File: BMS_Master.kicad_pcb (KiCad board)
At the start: 2 copper layers, 65 x 45 mm, 84 parts, among them J1 PWR, J2 PROG, J3 BMS_M_OUT, J4 BMS_M_IN, J5 CAN, Q1 BC807, SW1 SW_SPST, U1 AP2204K-ADJ, U2 AP2204K-ADJ, U3 STM32F103C8Tx, U4 BQ79600-Q1, U5 SN65HVD256D, Y1 8M, Y2 32.768k

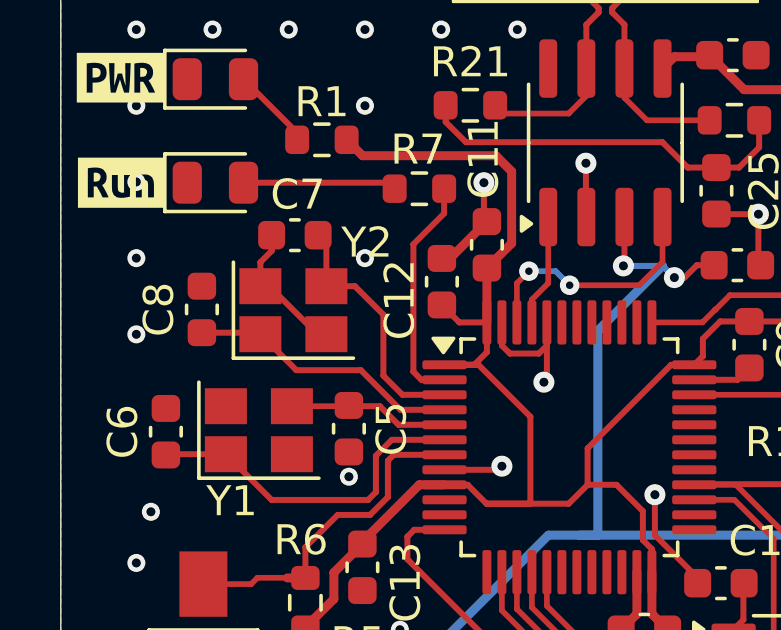
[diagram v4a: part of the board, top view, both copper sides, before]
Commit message: Fix crystal pinout connection
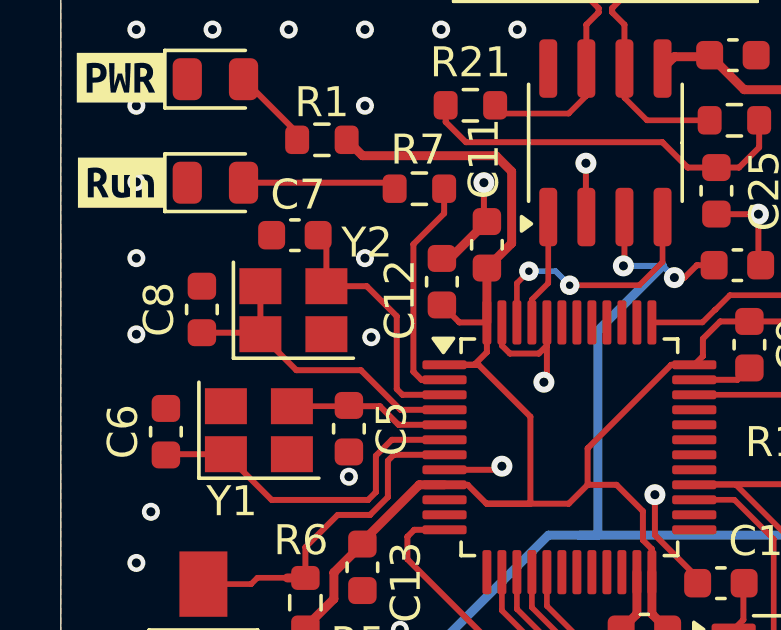
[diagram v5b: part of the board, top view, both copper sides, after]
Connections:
- net Net-(U3-PC14) renamed /LSE_IN
- C8 pad 1: Net-(U3-PC15) -> /LSE_OUT
- U3 pad 4: Net-(U3-PC15) -> /LSE_OUT
- Y2 pad 1: Net-(U3-PC15) -> /LSE_OUT
- Y2 pad 4: GND -> /LSE_OUT
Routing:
- net /LSE_OUT: track 0.00 -> 10.8 mm
- net Net-(U3-PC15): track 9.15 -> 0.00 mm
- net GND: track 37.1 -> 32.7 mm, vias 105 -> 106
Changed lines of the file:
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@@
   (net 5 "Net-(U3-PD0)")
   (net 6 "Net-(U3-PD1)")
-  (net 7 "Net-(U3-PC14)")
-  (net 8 "Net-(U3-PC15)")
+  (net 7 "/LSE_IN")
+  (net 8 "/LSE_OUT")
   (net 9 "Net-(U4-DVDD)")
   (net 10 "COMHP")
@@
       (stroke (width 0.1) (type solid)) (layer "F.Fab"))
     (pad "1" smd rect (at -1.1 0.8) (size 1.4 1.2) (layers "F.Cu" "F.Paste" "F.Mask")
-      (net 8 "Net-(U3-PC15)") (pinfunction "1") (pintype "passive"))
+      (net 8 "/LSE_OUT") (pinfunction "1") (pintype "passive"))
     (pad "2" smd rect (at 1.1 0.8) (size 1.4 1.2) (layers "F.Cu" "F.Paste" "F.Mask")
       (net 1 "GND") (pinfunction "2") (pintype "passive"))
     (pad "3" smd rect (at 1.1 -0.8) (size 1.4 1.2) (layers "F.Cu" "F.Paste" "F.Mask")
-      (net 7 "Net-(U3-PC14)") (pinfunction "3") (pintype "passive"))
+      (net 7 "/LSE_IN") (pinfunction "3") (pintype "passive"))
     (pad "4" smd rect (at -1.1 -0.8) (size 1.4 1.2) (layers "F.Cu" "F.Paste" "F.Mask")
-      (net 1 "GND") (pinfunction "4") (pintype "passive"))
+      (net 8 "/LSE_OUT") (pinfunction "4") (pintype "passive"))
     (model "${KICAD6_3DMODEL_DIR}/Crystal.3dshapes/Crystal_SMD_SeikoEpson_FA238-4Pin_3.2x2.5mm.wrl"
       (offset (xyz 0 0 0))
@@
       (net 33 "RUN_LED") (pinfunction "PC13") (pintype "bidirectional"))
     (pad "3" smd roundrect (at -4.1625 -1.75) (size 1.475 0.3) (layers "F.Cu" "F.Paste" "F.Mask") (roundrect_rratio 0.25)
-      (net 7 "Net-(U3-PC14)") (pinfunction "PC14") (pintype "bidirectional"))
+      (net 7 "/LSE_IN") (pinfunction "PC14") (pintype "bidirectional"))
     (pad "4" smd roundrect (at -4.1625 -1.25) (size 1.475 0.3) (layers "F.Cu" "F.Paste" "F.Mask") (roundrect_rratio 0.25)
-      (net 8 "Net-(U3-PC15)") (pinfunction "PC15") (pintype "bidirectional"))
+      (net 8 "/LSE_OUT") (pinfunction "PC15") (pintype "bidirectional"))
     (pad "5" smd roundrect (at -4.1625 -0.75) (size 1.475 0.3) (layers "F.Cu" "F.Paste" "F.Mask") (roundrect_rratio 0.25)
       (net 5 "Net-(U3-PD0)") (pinfunction "PD0") (pintype "bidirectional"))
@@
       (stroke (width 0.1) (type solid)) (layer "F.Fab"))
     (pad "1" smd roundrect (at -0.775 0 90) (size 0.9 0.95) (layers "F.Cu" "F.Paste" "F.Mask") (roundrect_rratio 0.25)
-      (net 8 "Net-(U3-PC15)") (pintype "passive"))
+      (net 8 "/LSE_OUT") (pintype "passive"))
     (pad "2" smd roundrect (at 0.775 0 90) (size 0.9 0.95) (layers "F.Cu" "F.Paste" "F.Mask") (roundrect_rratio 0.25)
       (net 1 "GND") (pintype "passive"))
@@
       (stroke (width 0.1) (type solid)) (layer "F.Fab"))
     (pad "1" smd roundrect (at -0.775 0 180) (size 0.9 0.95) (layers "F.Cu" "F.Paste" "F.Mask") (roundrect_rratio 0.25)
-      (net 7 "Net-(U3-PC14)") (pintype "passive"))
+      (net 7 "/LSE_IN") (pintype "passive"))
     (pad "2" smd roundrect (at 0.775 0 180) (size 0.9 0.95) (layers "F.Cu" "F.Paste" "F.Mask") (roundrect_rratio 0.25)
       (net 1 "GND") (pintype "passive"))
@@
   (segment (start 87.36 55.25) (end 87.355 55.245) (width 0.2) (layer "F.Cu") (net 1))
   (segment (start 80.085 63.77) (end 78.2925 63.77) (width 0.2) (layer "F.Cu") (net 1))
+  (segment (start 74.355 59.25) (end 74.055 59.25) (width 0.2) (layer "F.Cu") (net 1))
   (segment (start 84.705 68.575) (end 84.705 67.1825) (width 0.3) (layer "F.Cu") (net 1))
   (segment (start 85.305 64.6) (end 85.305 65.946904) (width 0.2) (layer "F.Cu") (net 1))
@@
   (segment (start 86.73 67.371904) (end 86.73 67.55) (width 0.2) (layer "F.Cu") (net 1))
   (segment (start 78.205 56.725) (end 78.475 56.725) (width 0.3) (layer "F.Cu") (net 1))
-  (segment (start 72.53 56.475) (end 72.53 55.95) (width 0.2) (layer "F.Cu") (net 1))
   (segment (start 81.705 58.8575) (end 81.705 59.62741) (width 0.2) (layer "F.Cu") (net 1))
   (segment (start 82.875 72.57) (end 83.405 73.1) (width 0.2) (layer "F.Cu") (net 1))
@@
   (segment (start 88.755 56.875) (end 88.83 56.95) (width 0.2) (layer "F.Cu") (net 1))
   (segment (start 79.605 55.395) (end 79.705 55.495) (width 0.2) (layer "F.Cu") (net 1))
-  (segment (start 72.155 56.85) (end 72.53 56.475) (width 0.2) (layer "F.Cu") (net 1))
   (segment (start 81.43741 59.895) (end 80.47259 59.895) (width 0.2) (layer "F.Cu") (net 1))
   (segment (start 84.955 70.4) (end 84.18 69.625) (width 0.2) (layer "F.Cu") (net 1))
   (segment (start 84.18 69.625) (end 84.18 69.1) (width 0.2) (layer "F.Cu") (net 1))
-  (segment (start 72.455 57.65) (end 74.055 59.25) (width 0.2) (layer "F.Cu") (net 1))
   (segment (start 83.005 53.55) (end 83.005 55.33) (width 0.2) (layer "F.Cu") (net 1))
   (segment (start 85.305 65.946904) (end 86.73 67.371904) (width 0.2) (layer "F.Cu") (net 1))
@@
   (segment (start 88.06 60.77) (end 86.6175 60.77) (width 0.2) (layer "F.Cu") (net 1))
   (segment (start 88.455 60.375) (end 88.06 60.77) (width 0.2) (layer "F.Cu") (net 1))
-  (segment (start 74.055 59.25) (end 74.355 59.25) (width 0.2) (layer "F.Cu") (net 1))
   (segment (start 95.355 74.07) (end 96.005 74.07) (width 0.2) (layer "F.Cu") (net 1))
   (segment (start 88.755 55.25) (end 88.755 56.875) (width 0.2) (layer "F.Cu") (net 1))
   (segment (start 81.155 76.7875) (end 81.155 78.175) (width 0.3) (layer "F.Cu") (net 1))
   (segment (start 81.705 59.62741) (end 81.43741 59.895) (width 0.2) (layer "F.Cu") (net 1))
-  (segment (start 72.155 57.65) (end 72.455 57.65) (width 0.2) (layer "F.Cu") (net 1))
-  (segment (start 72.155 57.65) (end 72.155 56.85) (width 0.2) (layer "F.Cu") (net 1))
   (segment (start 81.155 78.175) (end 81.43 78.45) (width 0.3) (layer "F.Cu") (net 1))
   (segment (start 81.705 60.75) (end 81.705 58.8575) (width 0.2) (layer "F.Cu") (net 1))
@@
   (via (at 70.56 74.495) (size 0.6) (drill 0.3) (layers "F.Cu" "B.Cu") (free) (net 1))
   (via (at 78.18 46.555) (size 0.6) (drill 0.3) (layers "F.Cu" "B.Cu") (free) (net 1))
+  (via (at 75.85 59.35) (size 0.6) (drill 0.3) (layers "F.Cu" "B.Cu") (free) (net 1))
   (segment (start 80.205 76.125001) (end 80.555001 75.775) (width 0.3) (layer "F.Cu") (net 2))
   (segment (start 80.205 76.7875) (end 80.205 76.125001) (width 0.3) (layer "F.Cu") (net 2))
@@
   (segment (start 72.53 64.775) (end 75.744798 64.775) (width 0.2) (layer "F.Cu") (net 6))
   (segment (start 76.535 62.77) (end 78.2925 62.77) (width 0.2) (layer "F.Cu") (net 6))
-  (segment (start 76.255 58.6) (end 76.255 60.634314) (width 0.2) (layer "F.Cu") (net 7))
   (segment (start 74.355 56.225) (end 74.08 55.95) (width 0.2) (layer "F.Cu") (net 7))
-  (segment (start 75.305 57.65) (end 76.255 58.6) (width 0.2) (layer "F.Cu") (net 7))
-  (segment (start 74.355 57.65) (end 75.305 57.65) (width 0.2) (layer "F.Cu") (net 7))
-  (segment (start 74.355 57.65) (end 74.355 56.225) (width 0.2) (layer "F.Cu") (net 7))
-  (segment (start 76.255 60.634314) (end 76.890686 61.27) (width 0.2) (layer "F.Cu") (net 7))
+  (segment (start 75.7 57.65) (end 76.7 58.65) (width 0.2) (layer "F.Cu") (net 7))
   (segment (start 76.890686 61.27) (end 78.2925 61.27) (width 0.2) (layer "F.Cu") (net 7))
+  (segment (start 76.7 58.65) (end 76.7 61.079314) (width 0.2) (layer "F.Cu") (net 7))
+  (segment (start 74.355 57.65) (end 74.355 56.225) (width 0.2) (layer "F.Cu") (net 7))
+  (segment (start 76.7 61.079314) (end 76.890686 61.27) (width 0.2) (layer "F.Cu") (net 7))
+  (segment (start 74.355 57.65) (end 75.7 57.65) (width 0.2) (layer "F.Cu") (net 7))
   (segment (start 78.2925 61.77) (end 76.825 61.77) (width 0.2) (layer "F.Cu") (net 8))
+  (segment (start 72.155 59.25) (end 72.155 57.65) (width 0.2) (layer "F.Cu") (net 8))
   (segment (start 73.355 60.45) (end 72.155 59.25) (width 0.2) (layer "F.Cu") (net 8))
   (segment (start 75.505 60.45) (end 73.355 60.45) (width 0.2) (layer "F.Cu") (net 8))

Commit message: Finish layout ver 1, already abandoned
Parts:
- added C26: 100n, Capacitor_SMD:C_0603_1608Metric, F.Cu at (97.2, 49.4)
- added C27: 100n, Capacitor_SMD:C_0603_1608Metric, F.Cu at (104.7, 49.4)
- added C28: 220n, Capacitor_SMD:C_0805_2012Metric, F.Cu at (98.5, 52.8)
- added C29: 220n, Capacitor_SMD:C_0805_2012Metric, F.Cu at (103.4, 52.8)
- added J6: Current_Sensor, Connector_JST:JST_XH_B4B-XH-A_1x04_P2.50mm_Vertical, F.Cu at (97.2, 44.7)
- added R23: 10K, Resistor_SMD:R_0603_1608Metric, F.Cu at (97.2, 51.0)
- added R24: 10K, Resistor_SMD:R_0603_1608Metric, F.Cu at (104.7, 51.0)
- added R25: 10K, Resistor_SMD:R_0603_1608Metric, F.Cu at (102.4, 50.2)
- added R26: 10K, Resistor_SMD:R_0603_1608Metric, F.Cu at (99.5, 50.2)
- moved kibuzzard-6797C095 11.9 mm to (120.3, 35.8)
- renumbered C25 to C24, C24 to C25
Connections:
- U3 pad 10: unconnected-(U3-PA0-Pad10) -> Current_Sensor_1
- U3 pad 11: unconnected-(U3-PA1-Pad11) -> Current_Sensor_2
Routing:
- net Current_Sensor_2: track 0.00 -> 42.2 mm, vias 0 -> 2
- net Current_Sensor_1: track 0.00 -> 41.5 mm, vias 0 -> 2
- net +5V: track 63.0 -> 80.9 mm
- net Net-(J6-Pin_2): track 0.00 -> 7.96 mm
- net Net-(J6-Pin_3): track 0.00 -> 7.92 mm
- net GND: track 32.7 -> 37.5 mm, vias 106 -> 92
- net VIO: track 139.6 -> 136.1 mm
- net BMS_FAULT: track 30.0 -> 28.4 mm
- net CAN_P: track 12.0 -> 11.2 mm
